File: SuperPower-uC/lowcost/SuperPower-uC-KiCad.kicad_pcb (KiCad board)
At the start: 2 copper layers, 83.6 x 28.2 mm, 82 parts, among them J1 Battery connector, J2 Thermistor, J3 USB_B_Micro, J4 Solar in, J5 main pin header right, J6 main pin header left, J7 expander pins nc, J8 expander pins, Q1 2N7002, Q2 2N7002, Q3 S8050, Q4 S8050, Q5 AO3401A, Q6 AO3401A, Q7 2N7002, U1 FS312F-G, U10 FP6291LR, U11 ME6210A33P, U12 ME6210A33P, U13 ESP32-WROOM32, U2 FS8205A, U3 LC709203FQH, U4 TP4056, U5 CH340G, U6 AMS1117-3.3, U7 PCF8563T, U8 XC6206P332MR, U9 TCA6408A, Y1 12MHZ, Y2 32.768KHz

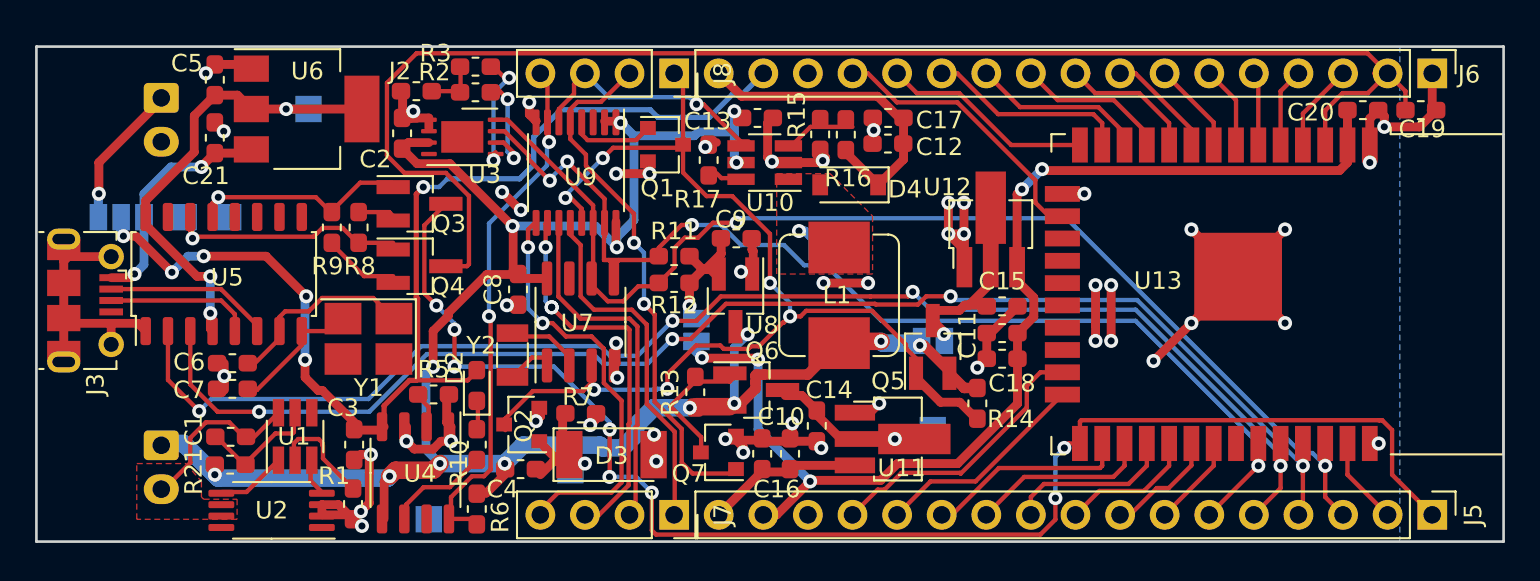
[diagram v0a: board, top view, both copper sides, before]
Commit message: connected external int pin to p0 of io expander
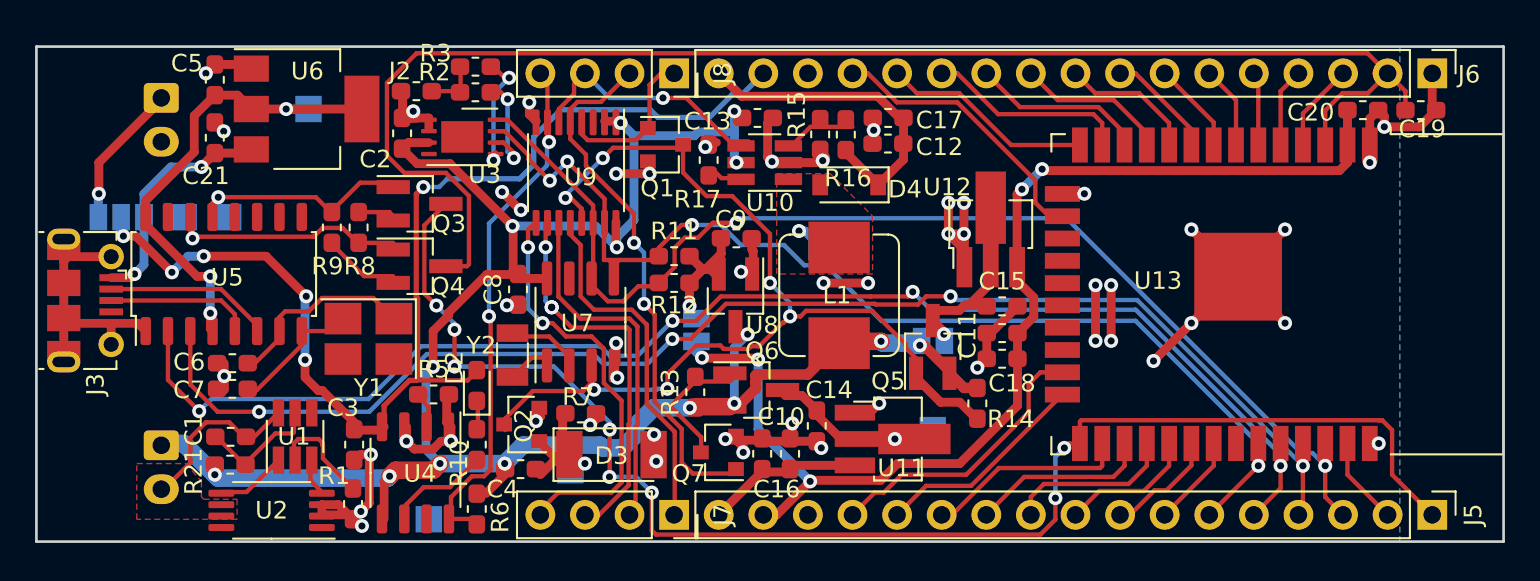
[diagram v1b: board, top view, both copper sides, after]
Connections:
- J8 pad 1: /Charging Module/INT -> /RTC and Cut-Off Module/INT_IO
- Q1 pad 1: Net-(Q1-Pad1) -> /RTC and Cut-Off Module/INT_IO
- U9 pad 4: Net-(Q1-Pad1) -> /RTC and Cut-Off Module/INT_IO
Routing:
- net /RTC and Cut-Off Module/INT_IO: track 0.00 -> 9.09 mm
- net Net-(Q1-Pad1): track 4.92 -> 0.00 mm
- net /Charging Module/INT: track 63.3 -> 59.1 mm

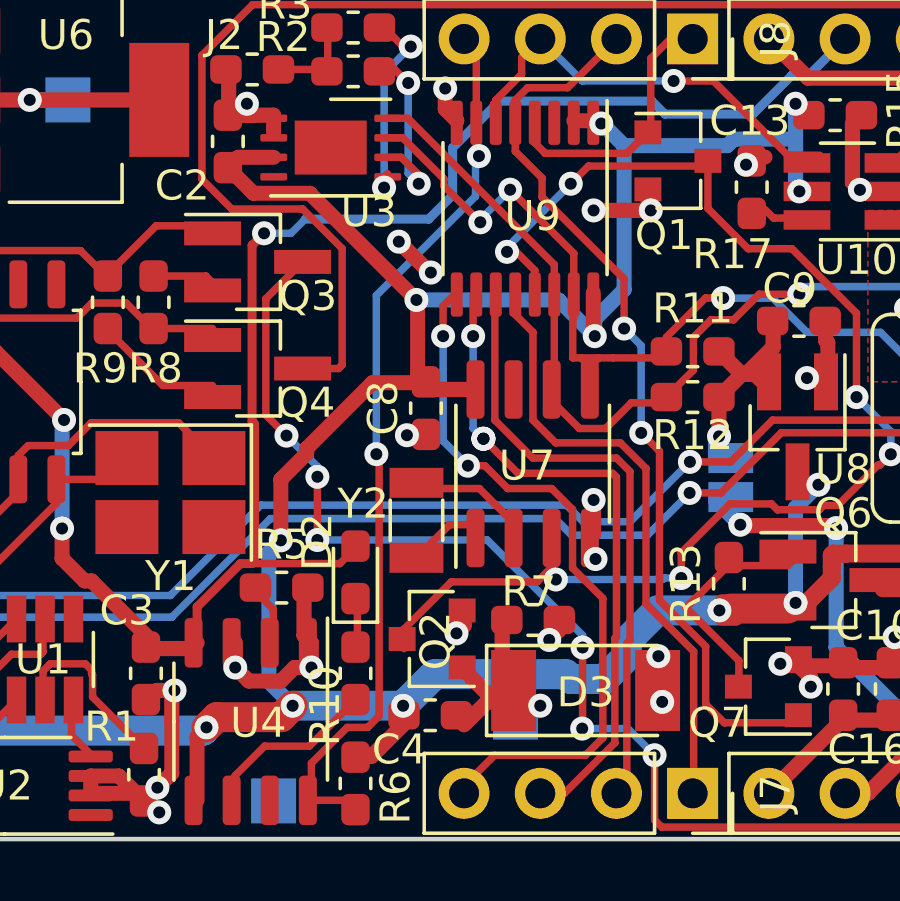
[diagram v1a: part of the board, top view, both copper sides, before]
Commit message: added testpoint and pcb stuff
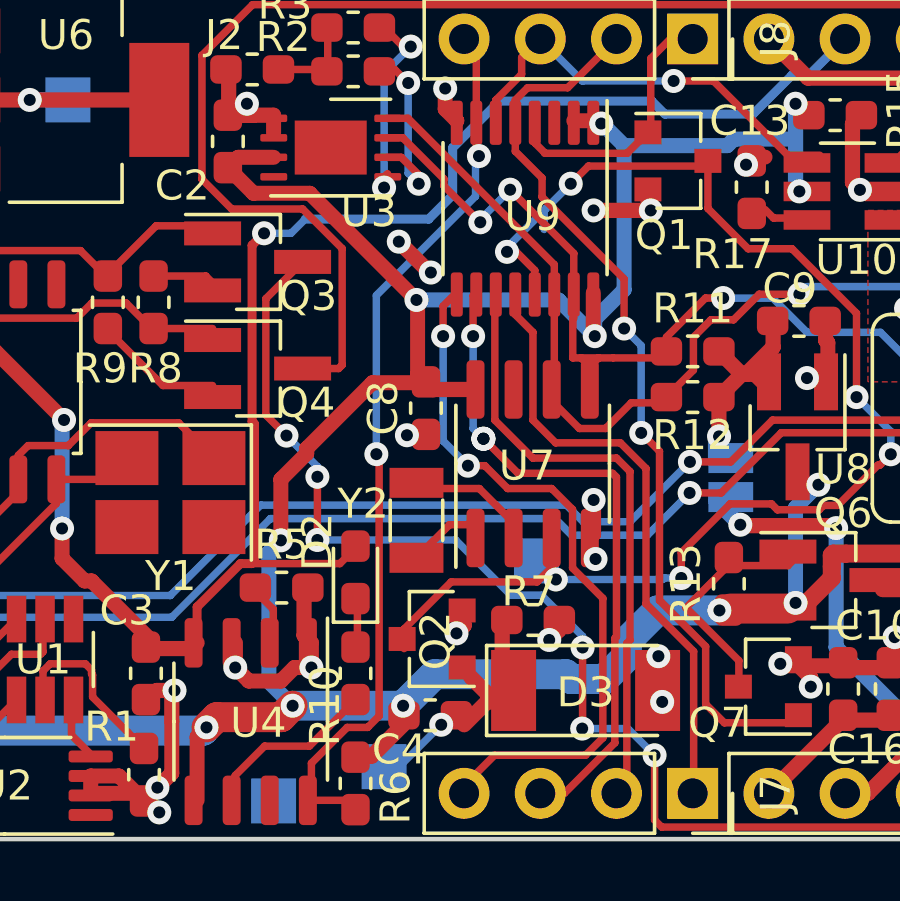
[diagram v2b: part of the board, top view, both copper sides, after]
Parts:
- added TP2: TestPoint, TestPoint:TestPoint_Pad_1.5x1.5mm, B.Cu at (133.1, 114.0)
- moved TP3 4.68 mm to (128.0, 120.9)
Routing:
- net /Charging Module/INT: track 59.1 -> 60.7 mm
- net Net-(C4-Pad2): track 9.33 -> 10.8 mm
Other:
- board text added: "CH_DIS"
- board text removed: "CH-DIS"
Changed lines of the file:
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@@
     (thickness 1.6)
     (drawings 51)
-    (tracks 1014)
+    (tracks 1023)
     (zones 0)
-    (modules 82)
+    (modules 83)
     (nets 95)
   )
   (page A4)
   (layers
-    (0 F.Cu signal)
-    (31 B.Cu signal)
-    (32 B.Adhes user)
-    (33 F.Adhes user)
-    (34 B.Paste user)
-    (35 F.Paste user)
+    (0 F.Cu signal hide)
+    (31 B.Cu signal hide)
+    (32 B.Adhes user hide)
+    (33 F.Adhes user hide)
+    (34 B.Paste user hide)
+    (35 F.Paste user hide)
     (36 B.SilkS user)
-    (37 F.SilkS user)
+    (37 F.SilkS user hide)
     (38 B.Mask user)
-    (39 F.Mask user)
+    (39 F.Mask user hide)
     (40 Dwgs.User user)
     (41 Cmts.User user)
@@
     (45 Margin user)
     (46 B.CrtYd user hide)
-    (47 F.CrtYd user)
+    (47 F.CrtYd user hide)
     (48 B.Fab user hide)
     (49 F.Fab user hide)
@@
     (add_net "Net-(U9-Pad3)")
   )
+  (module TestPoint:TestPoint_Pad_1.5x1.5mm (layer B.Cu)
+    (at 133.096 114.046)
+    (descr "SMD rectangular pad as test Point, square 1.5mm side length")
+    (tags "test point SMD pad rectangle square")
+    (attr virtual)
+    (fp_text reference TP2 (at 0.127 -2.413 90) (layer B.SilkS)
+      (effects (font (size 1 1) (thickness 0.15)) (justify mirror))
+    )
+    (fp_text value TestPoint (at 0 -1.75) (layer B.Fab)
+      (effects (font (size 1 1) (thickness 0.15)) (justify mirror))
+    )
+    (fp_text user %R (at 0 1.65) (layer B.Fab)
+      (effects (font (size 1 1) (thickness 0.15)) (justify mirror))
+    )
+    (fp_line (start -0.95 0.95) (end 0.95 0.95) (layer B.SilkS) (width 0.12))
+    (fp_line (start 0.95 0.95) (end 0.95 -0.95) (layer B.SilkS) (width 0.12))
+    (fp_line (start 0.95 -0.95) (end -0.95 -0.95) (layer B.SilkS) (width 0.12))
+    (fp_line (start -0.95 -0.95) (end -0.95 0.95) (layer B.SilkS) (width 0.12))
+    (fp_line (start -1.25 1.25) (end 1.25 1.25) (layer B.CrtYd) (width 0.05))
+    (fp_line (start -1.25 1.25) (end -1.25 -1.25) (layer B.CrtYd) (width 0.05))
+    (fp_line (start 1.25 -1.25) (end 1.25 1.25) (layer B.CrtYd) (width 0.05))
+    (fp_line (start 1.25 -1.25) (end -1.25 -1.25) (layer B.CrtYd) (width 0.05))
+    (pad 1 smd rect (at 0 0) (size 1.5 1.5) (layers B.Cu B.Mask)
+      (net 57 "/Charging Module/INT"))
+  )
   (module Connector_PinSocket_2.54mm:PinSocket_1x04_P2.54mm_Vertical (layer F.Cu)
     (at 138.303 96.647 270)
@@
   )
   (module TestPoint:TestPoint_Pad_1.5x1.5mm (layer B.Cu)
-    (at 132.3975 119.253)
+    (at 128.016 120.904)
     (descr "SMD rectangular pad as test Point, square 1.5mm side length")
     (tags "test point SMD pad rectangle square")
@@
     (effects (font (size 1 1) (thickness 0.15)) (justify mirror))
   )
-  (gr_text EXP4 (at 134.112 118.999 90) (layer B.SilkS)
+  (gr_text EXP4 (at 133.477 118.872 90) (layer B.SilkS)
     (effects (font (size 1 1) (thickness 0.15)) (justify mirror))
   )
@@
     (effects (font (size 1 1) (thickness 0.15)) (justify mirror))
   )
-  (gr_text CH-DIS (at 133.35 100.5205 90) (layer B.SilkS)
+  (gr_text CH_DIS (at 133.35 100.33 90) (layer B.SilkS)
     (effects (font (size 1 1) (thickness 0.15)) (justify mirror))
   )
@@
   (gr_line (start 101.981 95.123) (end 101.981 123.317) (layer Edge.Cuts) (width 0.15))
   (gr_line (start 185.547 95.123) (end 101.981 95.123) (layer Edge.Cuts) (width 0.15))
+  (via (at 129.921 119.507) (size 0.8) (drill 0.4) (layers F.Cu B.Cu) (net 6))
   (segment (start 110.744 118.832) (end 109.347 120.229) (width 0.25) (layer F.Cu) (net 1))
   (segment (start 110.744 117.4115) (end 110.744 118.832) (width 0.25) (layer F.Cu) (net 1))
@@
   (segment (start 131.953 116.205) (end 131.953 118.237) (width 0.508) (layer F.Cu) (net 6))
   (segment (start 132.334 118.364) (end 132.715 118.364) (width 0.25) (layer F.Cu) (net 6))
-  (segment (start 132.715 118.364) (end 133.223002 118.872002) (width 0.25) (layer F.Cu) (net 6))
-  (segment (start 132.3975 119.253) (end 132.778498 118.872002) (width 0.25) (layer B.Cu) (net 6))
-  (segment (start 132.778498 118.872002) (end 133.223002 118.872002) (width 0.25) (layer B.Cu) (net 6))
-  (via (at 133.223002 118.872002) (size 0.8) (drill 0.4) (layers F.Cu B.Cu) (net 6))
+  (segment (start 130.429 119.1895) (end 130.429 119.253) (width 0.25) (layer F.Cu) (net 6))
+  (segment (start 130.2385 119.1895) (end 129.921 119.507) (width 0.25) (layer F.Cu) (net 6))
+  (segment (start 130.429 119.1895) (end 130.2385 119.1895) (width 0.25) (layer F.Cu) (net 6))
+  (segment (start 128.524 120.904) (end 129.921 119.507) (width 0.25) (layer B.Cu) (net 6))
+  (segment (start 128.016 120.904) (end 128.524 120.904) (width 0.25) (layer B.Cu) (net 6))
   (via (at 116.205 98.679) (size 0.8) (drill 0.4) (layers F.Cu B.Cu) (net 7))
   (segment (start 114.223 98.679) (end 116.205 98.679) (width 0.508) (layer F.Cu) (net 7))
@@
   (segment (start 137.033 122.682) (end 137.033 120.523) (width 0.25) (layer F.Cu) (net 37))
   (via (at 134.633975 116.931263) (size 0.8) (drill 0.4) (layers F.Cu B.Cu) (net 37))
-  (segment (start 131.453152 113.3475) (end 134.633975 116.528323) (width 0.25) (layer B.Cu) (net 37))
-  (segment (start 134.633975 116.528323) (end 134.633975 116.931263) (width 0.25) (layer B.Cu) (net 37))
-  (segment (start 125.7935 113.3475) (end 131.453152 113.3475) (width 0.25) (layer B.Cu) (net 37))
   (segment (start 134.633975 119.620025) (end 134.62 119.634) (width 0.25) (layer F.Cu) (net 37))
   (segment (start 134.633975 116.931263) (end 134.633975 119.620025) (width 0.25) (layer F.Cu) (net 37))
@@
   (segment (start 137.033 120.523) (end 136.144 119.634) (width 0.25) (layer B.Cu) (net 37))
   (segment (start 136.144 119.634) (end 134.62 119.634) (width 0.25) (layer B.Cu) (net 37))
+  (segment (start 134.633975 116.55468) (end 134.633975 116.931263) (width 0.25) (layer B.Cu) (net 37))
+  (segment (start 133.268295 115.189) (end 134.633975 116.55468) (width 0.25) (layer B.Cu) (net 37))
+  (segment (start 132.243998 115.189) (end 133.268295 115.189) (width 0.25) (layer B.Cu) (net 37))
+  (segment (start 130.402498 113.3475) (end 132.243998 115.189) (width 0.25) (layer B.Cu) (net 37))
+  (segment (start 125.7935 113.3475) (end 130.402498 113.3475) (width 0.25) (layer B.Cu) (net 37))
   (segment (start 149.338132 96.647) (end 148.463 96.647) (width 0.25) (layer F.Cu) (net 38))
   (segment (start 150.989132 98.298) (end 149.338132 96.647) (width 0.25) (layer F.Cu) (net 38))
@@
   (via (at 132.113414 103.742733) (size 0.8) (drill 0.4) (layers F.Cu B.Cu) (net 57))
   (segment (start 132.113414 103.598586) (end 132.113414 103.742733) (width 0.25) (layer B.Cu) (net 57))
-  (segment (start 134.239 101.473) (end 132.113414 103.598586) (width 0.25) (layer B.Cu) (net 57))
   (segment (start 132.422733 103.742733) (end 132.113414 103.742733) (width 0.25) (layer F.Cu) (net 57))
   (via (at 143.764 108.585) (size 0.8) (drill 0.4) (layers F.Cu B.Cu) (net 57))
@@
   (segment (start 145.504996 110.490002) (end 145.822498 110.1725) (width 0.25) (layer F.Cu) (net 57))
   (segment (start 144.907 110.490002) (end 145.504996 110.490002) (width 0.25) (layer F.Cu) (net 57))
+  (segment (start 133.35 102.362) (end 133.4135 102.2985) (width 0.25) (layer B.Cu) (net 57))
+  (segment (start 133.35 102.997) (end 133.35 102.362) (width 0.25) (layer B.Cu) (net 57))
+  (segment (start 133.4135 102.2985) (end 132.113414 103.598586) (width 0.25) (layer B.Cu) (net 57))
+  (segment (start 134.239 101.473) (end 133.4135 102.2985) (width 0.25) (layer B.Cu) (net 57))
+  (segment (start 133.714469 114.664469) (end 133.096 114.046) (width 0.25) (layer B.Cu) (net 57))
+  (segment (start 133.742766 114.664469) (end 133.714469 114.664469) (width 0.25) (layer B.Cu) (net 57))
   (segment (start 133.04 99.3725) (end 133.04 100.11) (width 0.25) (layer F.Cu) (net 94))
   (segment (start 133.04 100.11) (end 133.365009 100.435009) (width 0.25) (layer F.Cu) (net 94))
